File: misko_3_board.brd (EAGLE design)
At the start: 96 x 162 mm, 177 parts, among them IC1 ATMEGA1281-16AU, IC10 ORG1510-MK4, IC11 TPS3808G33DBVT, IC12 LTC4425, IC13 RN-42, IC14 ADXL345, IC15 74HCT1G32, IC16 FM25W256-SOIC, IC17 MICROSD_SPI_MODE, IC18 FH12-30S-0.5SH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

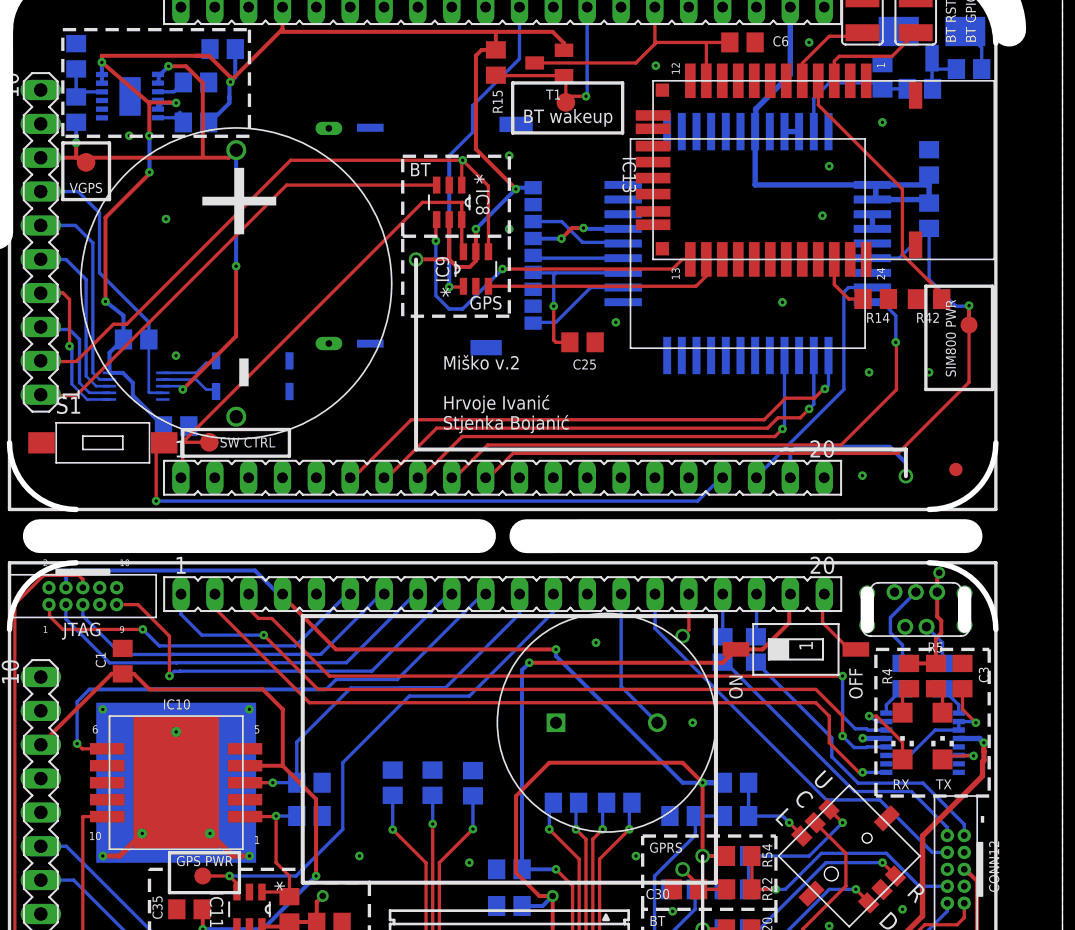
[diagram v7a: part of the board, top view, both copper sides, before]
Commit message: - updated libraries & generated new gerber files
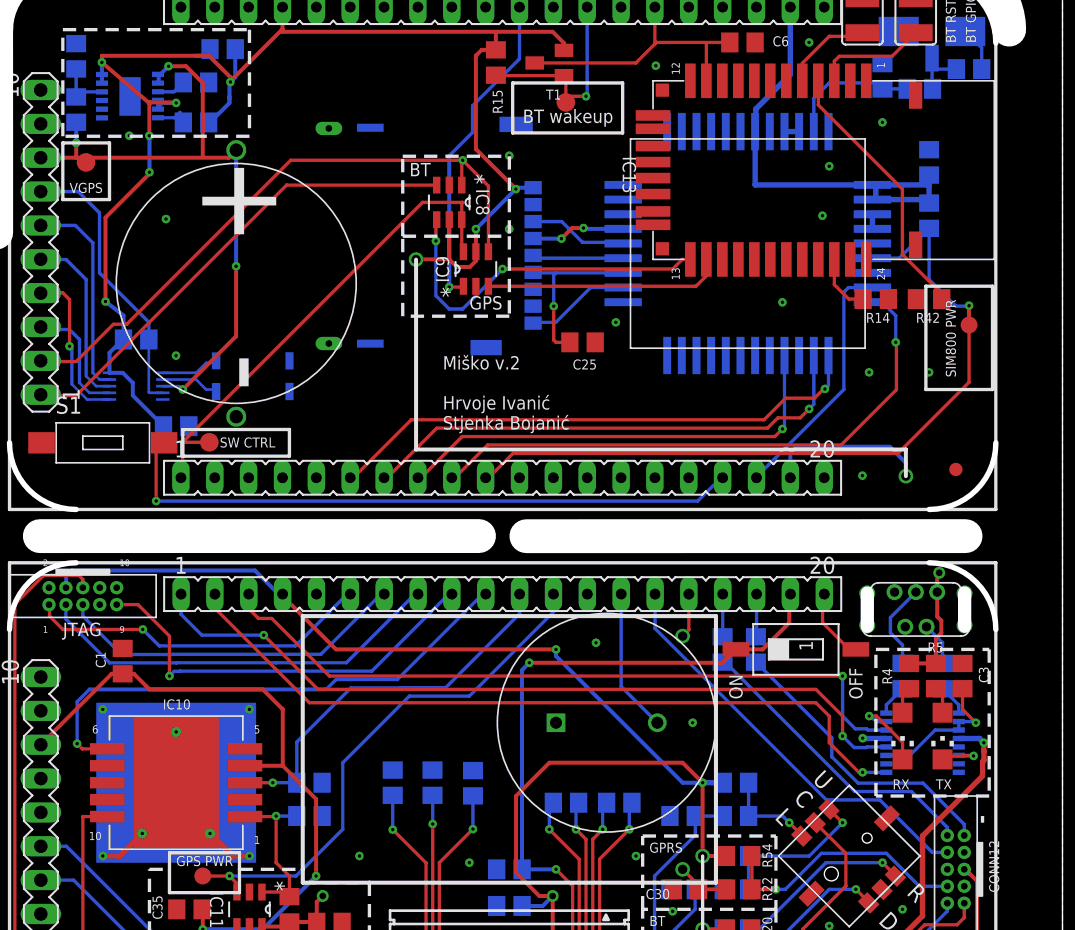
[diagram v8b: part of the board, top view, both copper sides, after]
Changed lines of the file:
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@@
 <wire x1="14.5" y1="120" x2="14.5" y2="114.5" width="0.3" layer="1"/>
 <contactref element="R60" pad="2"/>
-<wire x1="11.9308" y1="121.255" x2="11.9308" y2="122.5192" width="0" layer="19" extent="1-16"/>
 <wire x1="5" y1="114.39" x2="5" y2="115.5" width="0.3" layer="1"/>
 <via x="5" y="115.5" extent="1-16" drill="0.25"/>
